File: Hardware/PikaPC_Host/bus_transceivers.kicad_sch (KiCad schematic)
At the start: 18 parts, among them U10 IDT74ALVC164245, U11 IDT74ALVC164245, U12 IDT74ALVC164245, U7 IDT74ALVC164245, U8 IDT74ALVC164245, U9 IDT74ALVC164245

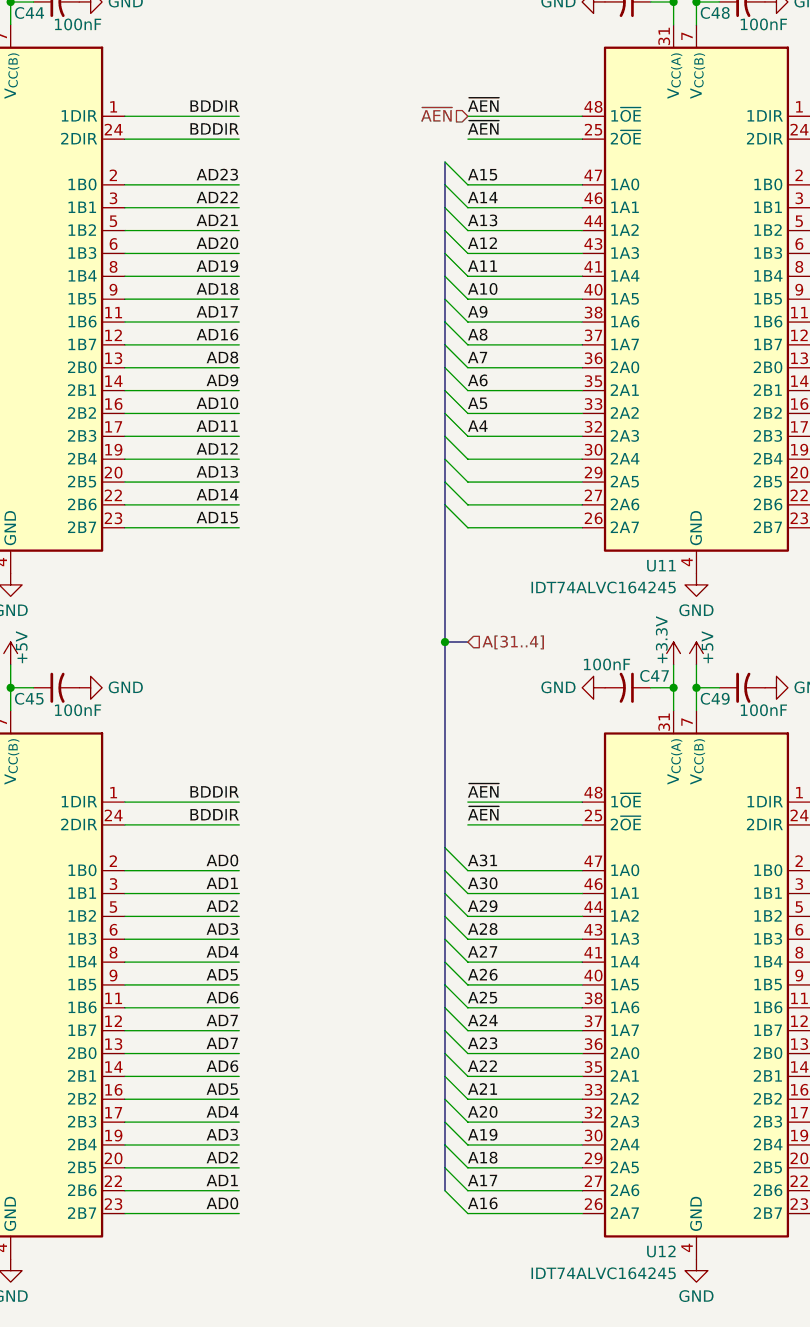
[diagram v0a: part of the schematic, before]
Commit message: Host card PCB layout
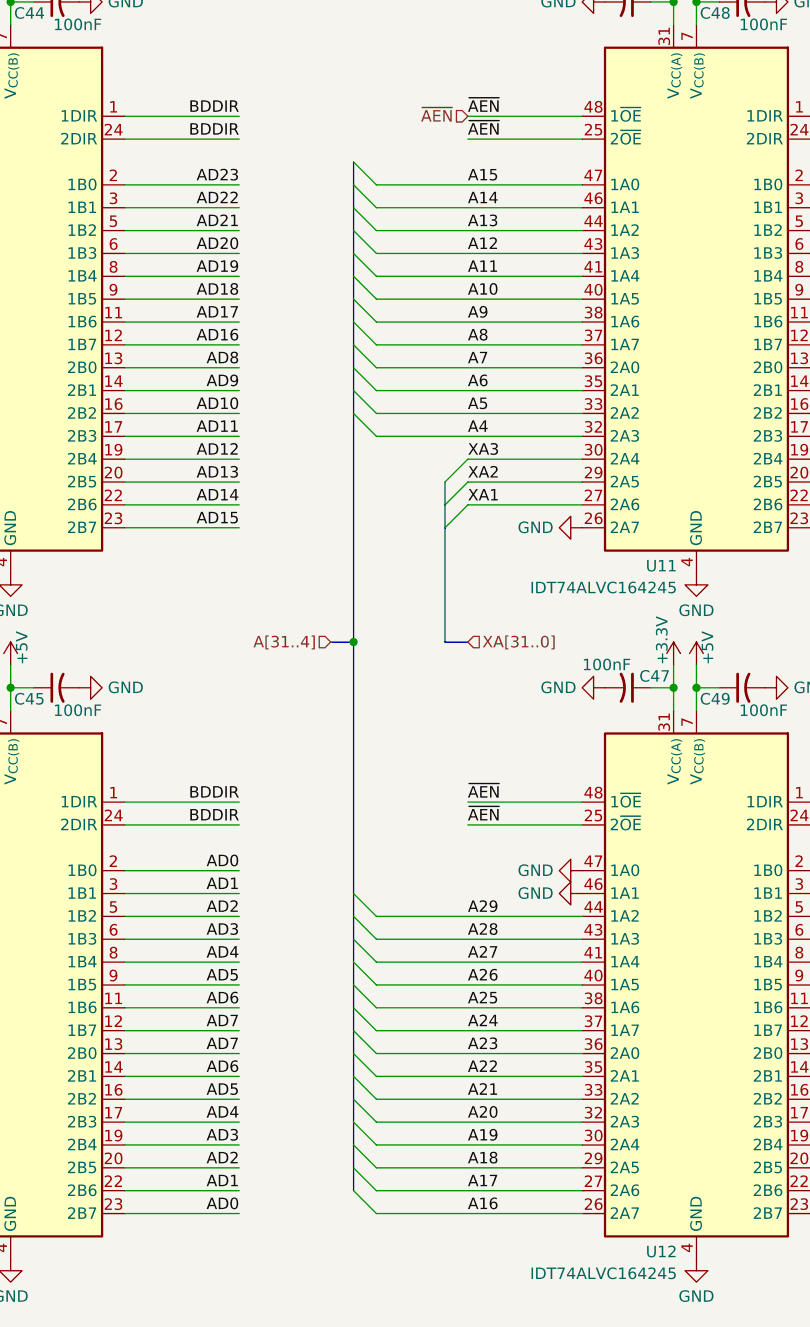
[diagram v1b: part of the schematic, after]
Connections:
- net A30 is gone; now on net GND: U12.46 (1A1)
- net A31 is gone; now on net GND: U12.47 (1A0)
- net GND: now also U11.26 (2A7)
- net XA1: now reaches U11.27 (2A6)
- net XA2: now reaches U11.29 (2A5)
- net XA3: now reaches U11.30 (2A4)

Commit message: Host Card refinement
add main bus clock selection
silkscreen cleanup
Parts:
- U10, U11, U12, U7, U8, U9: value IDT74ALVC164245 -> 74ALVC164245
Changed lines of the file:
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@@
 			)
 		)
-		(property "Value" "IDT74ALVC164245"
+		(property "Value" "74ALVC164245"
 			(at 124.8567 90.5044 0)
 			(effects
@@
 			)
 		)
-		(property "Value" "IDT74ALVC164245"
+		(property "Value" "74ALVC164245"
 			(at 48.6567 166.7044 0)
 			(effects
@@
 			)
 		)
-		(property "Value" "IDT74ALVC164245"
+		(property "Value" "74ALVC164245"
 			(at 124.8567 166.7044 0)
 			(effects
@@
 			)
 		)
-		(property "Value" "IDT74ALVC164245"
+		(property "Value" "74ALVC164245"
 			(at 48.6567 90.5044 0)
 			(effects
@@
 			)
 		)
-		(property "Value" "IDT74ALVC164245"
+		(property "Value" "74ALVC164245"
 			(at 201.0567 166.7044 0)
 			(effects
@@
 			)
 		)
-		(property "Value" "IDT74ALVC164245"
+		(property "Value" "74ALVC164245"
 			(at 201.0567 90.5044 0)
 			(effects

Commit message: Annotate & prep for output - Host & KBC
add gerber output to gitignore
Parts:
- C38, C39, C40, C41, C42, C43, C44, C45, C46, C47, C48, C49: Mouser (none) -> 187-CL21B104KACNNNC
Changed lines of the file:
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@@
 			)
 		)
+		(property "Mouser" "187-CL21B104KACNNNC"
+			(at 43.18 25.4 90)
+			(effects
+				(font
+					(size 1.27 1.27)
+				)
+				(hide yes)
+			)
+		)
 		(pin "2"
 		)
@@
 			)
 		)
+		(property "Mouser" "187-CL21B104KACNNNC"
+			(at 195.58 101.6 90)
+			(effects
+				(font
+					(size 1.27 1.27)
+				)
+				(hide yes)
+			)
+		)
 		(pin "2"
 		)
@@
 			)
 		)
+		(property "Mouser" "187-CL21B104KACNNNC"
+			(at 55.88 25.4 90)
+			(effects
+				(font
+					(size 1.27 1.27)
+				)
+				(hide yes)
+			)
+		)
 		(pin "2"
 		)
@@
 			)
 		)
+		(property "Mouser" "187-CL21B104KACNNNC"
+			(at 119.38 25.4 90)
+			(effects
+				(font
+					(size 1.27 1.27)
+				)
+				(hide yes)
+			)
+		)
 		(pin "2"
 		)
@@
 			)
 		)
+		(property "Mouser" "187-CL21B104KACNNNC"
+			(at 132.08 101.6 90)
+			(effects
+				(font
+					(size 1.27 1.27)
+				)
+				(hide yes)
+			)
+		)
 		(pin "2"
 		)
@@
 			)
 		)
+		(property "Mouser" "187-CL21B104KACNNNC"
+			(at 208.28 25.4 90)
+			(effects
+				(font
+					(size 1.27 1.27)
+				)
+				(hide yes)
+			)
+		)
 		(pin "2"
 		)
@@
 			)
 		)
+		(property "Mouser" "187-CL21B104KACNNNC"
+			(at 119.38 101.6 90)
+			(effects
+				(font
+					(size 1.27 1.27)
+				)
+				(hide yes)
+			)
+		)
 		(pin "2"
 		)
@@
 			)
 		)
+		(property "Mouser" "187-CL21B104KACNNNC"
+			(at 208.28 101.6 90)
+			(effects
+				(font
+					(size 1.27 1.27)
+				)
+				(hide yes)
+			)
+		)
 		(pin "2"
 		)
@@
 			)
 		)
+		(property "Mouser" "187-CL21B104KACNNNC"
+			(at 55.88 101.6 90)
+			(effects
+				(font
+					(size 1.27 1.27)
+				)
+				(hide yes)
+			)
+		)
 		(pin "2"
 		)
@@
 			)
 		)
+		(property "Mouser" "187-CL21B104KACNNNC"
+			(at 195.58 25.4 90)
+			(effects
+				(font
+					(size 1.27 1.27)
+				)
+				(hide yes)
+			)
+		)
 		(pin "2"
 		)
@@
 			)
 		)
+		(property "Mouser" "187-CL21B104KACNNNC"
+			(at 43.18 101.6 90)
+			(effects
+				(font
+					(size 1.27 1.27)
+				)
+				(hide yes)
+			)
+		)
 		(pin "2"
 		)
@@
 			(effects
 				(font
+					(size 1.27 1.27)
+				)
+				(hide yes)
+			)
+		)
+		(property "Mouser" "187-CL21B104KACNNNC"
+			(at 132.08 25.4 90)
+			(effects
+				(font

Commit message: fix low two expansion bus address bits
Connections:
- net GND: no longer U12.46 (1A1), U12.47 (1A0)
- new net XA30: U12.46 (1A1)
- new net XA31: U12.47 (1A0)
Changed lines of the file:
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@@
 	)
 	(junction
+		(at 175.26 96.52)
+		(diameter 0)
+		(color 0 0 0 0)
+	)
+	(junction
 		(at 127 101.6)
 		(diameter 0)
@@
 	)
 	(bus_entry
+		(at 175.26 119.38)
+		(size 2.54 2.54)
+		(stroke
+			(width 0)
+			(type default)
+		)
+	)
+	(bus_entry
 		(at 177.8 76.2)
 		(size -2.54 2.54)
@@
 	)
 	(bus_entry
+		(at 175.26 121.92)
+		(size 2.54 2.54)
+		(stroke
+			(width 0)
+			(type default)
+		)
+	)
+	(bus_entry
 		(at 22.86 149.86)
 		(size 2.54 2.54)
@@
 	(bus
 		(pts
+			(xy 175.26 96.52) (xy 175.26 119.38)
+		)
+		(stroke
+			(width 0)
+			(type default)
+		)
+	)
+	(bus
+		(pts
 			(xy 78.74 160.02) (xy 78.74 157.48)
 		)
@@
 		)
 	)
+	(bus
+		(pts
+			(xy 175.26 119.38) (xy 175.26 121.92)
+		)
+		(stroke
+			(width 0)
+			(type default)
+		)
+	)
 	(wire
 		(pts
@@
 	(wire
 		(pts
+			(xy 177.8 124.46) (xy 190.5 124.46)
+		)
+		(stroke
+			(width 0)
+			(type default)
+		)
+	)
+	(wire
+		(pts
 			(xy 139.7 68.58) (xy 152.4 68.58)
 		)
@@
 		)
 	)
+	(wire
+		(pts
+			(xy 177.8 121.92) (xy 190.5 121.92)
+		)
+		(stroke
+			(width 0)
+			(type default)
+		)
+	)
 	(bus
 		(pts
@@
 		)
 	)
+	(label "XA31"
+		(at 177.8 121.92 0)
+		(effects
+			(font
+				(size 1.27 1.27)
+			)
+			(justify left bottom)
+		)
+	)
 	(label "A26"
 		(at 177.8 134.62 0)
@@
 		)
 	)
+	(label "XA30"
+		(at 177.8 124.46 0)
+		(effects
+			(font
+				(size 1.27 1.27)
+			)
+			(justify left bottom)
+		)
+	)
 	(label "D12"
 		(at 25.4 76.2 0)
@@
 	)
 	(symbol
-		(lib_id "power:GND")
-		(at 190.5 124.46 270)
-		(mirror x)
-		(unit 1)
-		(exclude_from_sim no)
-		(in_bom yes)
-		(on_board yes)
-		(dnp no)
-		(fields_autoplaced yes)
-		(property "Reference" "#PWR0135"
-			(at 184.15 124.46 0)
-			(effects
-				(font
-					(size 1.27 1.27)
-				)
-				(hide yes)
-			)
-		)
-		(property "Value" "GND"
-			(at 187.3251 124.46 90)
-			(effects
-				(font
-					(size 1.27 1.27)
-				)
-				(justify right)
-			)
-		)
-		(property "Footprint" ""
-			(at 190.5 124.46 0)
-			(effects
-				(font
-					(size 1.27 1.27)
-				)
-				(hide yes)
-			)
-		)
-		(property "Datasheet" ""
-			(at 190.5 124.46 0)
-			(effects
-				(font
-					(size 1.27 1.27)
-				)
-				(hide yes)
-			)
-		)
-		(property "Description" "Power symbol creates a global label with name \"GND\" , ground"
-			(at 190.5 124.46 0)
-			(effects
-				(font
-					(size 1.27 1.27)
-				)
-				(hide yes)
-			)
-		)
-		(pin "1"
-		)
-		(instances
-			(project "PikaPC_Host"
-				(path "/6a60ec03-e28d-46ba-8906-3c4e1028fc94/541b8728-35ef-42a9-8317-6c507b38c6a8/54e771b3-bd6f-4e0c-8f12-389c897bcc13"
-					(reference "#PWR0135")
-					(unit 1)
-				)
-			)
-		)
-	)
-	(symbol
 		(lib_id "power:+5V")
 		(at 127 22.86 0)
@@
 					(unit 1)
 				)
-			)
-		)
-	)
-	(symbol
-		(lib_id "power:GND")
-		(at 190.5 121.92 270)
-		(mirror x)
-		(unit 1)
-		(exclude_from_sim no)
-		(in_bom yes)
-		(on_board yes)
-		(dnp no)
-		(fields_autoplaced yes)
-		(property "Reference" "#PWR0134"
-			(at 184.15 121.92 0)
-			(effects
-				(font
-					(size 1.27 1.27)
-				)
-				(hide yes)
-			)
-		)
-		(property "Value" "GND"
-			(at 187.3251 121.92 90)
-			(effects
-				(font
-					(size 1.27 1.27)
-				)
-				(justify right)
-			)
-		)
-		(property "Footprint" ""
-			(at 190.5 121.92 0)
-			(effects
-				(font
-					(size 1.27 1.27)
-				)
-				(hide yes)
-			)
-		)
-		(property "Datasheet" ""
-			(at 190.5 121.92 0)
-			(effects
-				(font
-					(size 1.27 1.27)
-				)
-				(hide yes)
-			)
-		)
-		(property "Description" "Power symbol creates a global label with name \"GND\" , ground"
-			(at 190.5 121.92 0)
-			(effects
-				(font
-					(size 1.27 1.27)
-				)
-				(hide yes)
-			)
-		)
-		(pin "1"
-		)
-		(instances
-			(project "PikaPC_Host"
-				(path "/6a60ec03-e28d-46ba-8906-3c4e1028fc94/541b8728-35ef-42a9-8317-6c507b38c6a8/54e771b3-bd6f-4e0c-8f12-389c897bcc13"
-					(reference "#PWR0134")
-					(unit 1)
-				)

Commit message: Host card should not route A4/A5 to expansion bus
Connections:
- net A4 is gone; now on net GND: U11.32 (2A3)
- net A5 is gone; now on net GND: U11.33 (2A2)
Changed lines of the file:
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@@
 	)
 	(bus_entry
-		(at 165.1 71.12)
-		(size 2.54 2.54)
-		(stroke
-			(width 0)
-			(type default)
-		)
-	)
-	(bus_entry
 		(at 165.1 144.78)
 		(size 2.54 2.54)
@@
 	)
 	(bus_entry
-		(at 165.1 68.58)
-		(size 2.54 2.54)
-		(stroke
-			(width 0)
-			(type default)
-		)
-	)
-	(bus_entry
 		(at 22.86 43.18)
 		(size 2.54 2.54)
@@
 	(bus
 		(pts
-			(xy 165.1 66.04) (xy 165.1 68.58)
+			(xy 165.1 66.04) (xy 165.1 96.52)
 		)
 		(stroke
@@
 	(wire
 		(pts
-			(xy 167.64 73.66) (xy 190.5 73.66)
-		)
-		(stroke
-			(width 0)
-			(type default)
-		)
-	)
-	(wire
-		(pts
 			(xy 167.64 55.88) (xy 190.5 55.88)
 		)
@@
 		)
 	)
-	(bus
-		(pts
-			(xy 165.1 71.12) (xy 165.1 96.52)
-		)
-		(stroke
-			(width 0)
-			(type default)
-		)
-	)
 	(wire
 		(pts
@@
 		)
 	)
-	(bus
-		(pts
-			(xy 165.1 68.58) (xy 165.1 71.12)
-		)
-		(stroke
-			(width 0)
-			(type default)
-		)
-	)
 	(wire
 		(pts
@@
 	(wire
 		(pts
-			(xy 167.64 71.12) (xy 190.5 71.12)
-		)
-		(stroke
-			(width 0)
-			(type default)
-		)
-	)
-	(wire
-		(pts
 			(xy 203.2 99.06) (xy 203.2 101.6)
 		)
@@
 		)
 	)
-	(label "A5"
-		(at 177.8 71.12 0)
-		(effects
-			(font
-				(size 1.27 1.27)
-			)
-			(justify left bottom)
-		)
-	)
 	(label "A23"
 		(at 177.8 142.24 0)
@@
 		)
 	)
-	(label "A4"
-		(at 177.8 73.66 0)
-		(effects
-			(font
-				(size 1.27 1.27)
-			)
-			(justify left bottom)
-		)
-	)
 	(label "AD29"
 		(at 76.2 50.8 180)
@@
 	(symbol
 		(lib_id "power:GND")
+		(at 190.5 73.66 270)
+		(mirror x)
+		(unit 1)
+		(exclude_from_sim no)
+		(in_bom yes)
+		(on_board yes)
+		(dnp no)
+		(fields_autoplaced yes)
+		(property "Reference" "#PWR0178"
+			(at 184.15 73.66 0)
+			(effects
+				(font
+					(size 1.27 1.27)
+				)
+				(hide yes)
+			)
+		)
+		(property "Value" "GND"
+			(at 187.3251 73.66 90)
+			(effects
+				(font
+					(size 1.27 1.27)
+				)
+				(justify right)
+			)
+		)
+		(property "Footprint" ""
+			(at 190.5 73.66 0)
+			(effects
+				(font
+					(size 1.27 1.27)
+				)
+				(hide yes)
+			)
+		)
+		(property "Datasheet" ""
+			(at 190.5 73.66 0)
+			(effects
+				(font
+					(size 1.27 1.27)
+				)
+				(hide yes)
+			)
+		)
+		(property "Description" "Power symbol creates a global label with name \"GND\" , ground"
+			(at 190.5 73.66 0)
+			(effects
+				(font
+					(size 1.27 1.27)
+				)
+				(hide yes)
+			)
+		)
+		(pin "1"
+		)
+		(instances
+			(project "PikaPC_Host"
+				(path "/6a60ec03-e28d-46ba-8906-3c4e1028fc94/541b8728-35ef-42a9-8317-6c507b38c6a8/54e771b3-bd6f-4e0c-8f12-389c897bcc13"
+					(reference "#PWR0178")
+					(unit 1)
+				)
+			)
+		)
+	)
+	(symbol
+		(lib_id "power:GND")
 		(at 134.62 101.6 90)
 		(unit 1)
@@
 					(unit 1)
 				)
+			)
+		)
+	)
+	(symbol
+		(lib_id "power:GND")
+		(at 190.5 71.12 270)
+		(mirror x)
+		(unit 1)
+		(exclude_from_sim no)
+		(in_bom yes)
+		(on_board yes)
+		(dnp no)
+		(fields_autoplaced yes)
+		(property "Reference" "#PWR0177"
+			(at 184.15 71.12 0)
+			(effects
+				(font
+					(size 1.27 1.27)
+				)
+				(hide yes)
+			)
+		)
+		(property "Value" "GND"
+			(at 187.3251 71.12 90)
+			(effects
+				(font
+					(size 1.27 1.27)
+				)
+				(justify right)
+			)
+		)
+		(property "Footprint" ""
+			(at 190.5 71.12 0)
+			(effects
+				(font
+					(size 1.27 1.27)
+				)
+				(hide yes)
+			)
+		)
+		(property "Datasheet" ""
+			(at 190.5 71.12 0)
+			(effects
+				(font
+					(size 1.27 1.27)
+				)
+				(hide yes)
+			)
+		)
+		(property "Description" "Power symbol creates a global label with name \"GND\" , ground"
+			(at 190.5 71.12 0)
+			(effects
+				(font
+					(size 1.27 1.27)
+				)
+				(hide yes)
+			)
+		)
+		(pin "1"
+		)
+		(instances
+			(project "PikaPC_Host"
+				(path "/6a60ec03-e28d-46ba-8906-3c4e1028fc94/541b8728-35ef-42a9-8317-6c507b38c6a8/54e771b3-bd6f-4e0c-8f12-389c897bcc13"
+					(reference "#PWR0177")
+					(unit 1)
+				)
